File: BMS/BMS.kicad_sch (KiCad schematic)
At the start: 112 parts, among them IC1 L9963E-TR, T1 Transformer_1P_1S, T2 Transformer_1P_1S, U1 QRE1113GR

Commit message: Setting up footprint and model library
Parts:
- removed RDIS14: 39, symbol Device:R_US
- removed RLPF14, RLPF15: 100, symbol Device:R_US
- added R1, R2: 100, symbol test:RC0603FR-07100RL
- added R3: 39, symbol 39R0603:RC0603FR-0739RL
- IC1: footprint QFP50P1200X1200X120-65N -> R4_standard_footprints:QFP50P1200X1200X120-65N
- renumbered 10uf to 10uf1, 33pf to 33pf1, 4.7uf to 4.7uf1, 68nf to 68nf1, CBAT_3 to CBAT_1, CBAT_1 to CBAT_3, CBOOT to CBOOT1, CESD15 to CESD1, CESD4 to CESD10, CESD3 to CESD11, CESD5 to CESD12, CESD17 to CESD13, CESD2 to CESD14, CESD12 to CESD15, CESD7 to CESD16, CESD13 to CESD17, CESD16 to CESD2, CESD11 to CESD3, CESD10 to CESD4, CESD9 to CESD5, CESD8 to CESD6, CESD6 to CESD7, CESD18 to CESD8, CESD19 to CESD9, CFLTH to CFLTH1, CLPF13 to CLPF1, CLPF4 to CLPF10, CLPF5 to CLPF11, CLPF10 to CLPF12, CLPF6 to CLPF13, CLPF12 to CLPF2, CLPF11 to CLPF3, CLPF1 to CLPF4, CLPF2 to CLPF5, CLPF7 to CLPF6, CLPF3 to CLPF7, CNPN to CNPN1, CNTC to CNTC1, CNTC4 to CNTC3, CNTC5 to CNTC4, CNTC1 to CNTC5, CNTC3 to CNTC6, CNTC6 to CNTC7, CVANA to CVANA1, CVCOM to CVCOM1, CVTREF to CVTREF1, DOPT to DOPT1, DZBAT to DZBAT1, DZBAT to DZBAT2, FR_BAT to FR_BAT1, MREG to MREG1, RBAT_DOWN to RBAT_DOWN1, RBAT_UP to RBAT_UP1, RDIS4 to RDIS10, RDIS5 to RDIS11, RDIS3 to RDIS12, RDIS2 to RDIS13, RDIS1 to RDIS14, RDIS12 to RDIS2, RDIS13 to RDIS3, RDIS10 to RDIS4, RDIS11 to RDIS5, RDIS8 to RDIS6, RDIS9 to RDIS7, RDIS6 to RDIS8, RDIS7 to RDIS9, RFAULTL to RFAULTL1, RFAULT_DOWN to RFAULT_DOWN1, RFLT to RFLT1, RFLT_PD to RFLT_PD1, RGPIO to RGPIO1, RGPIO4 to RGPIO3, RGPIO5 to RGPIO4, RGPIO1 to RGPIO5, RGPIO3 to RGPIO6, RGPIO6 to RGPIO7, RI_Sense to RI_Sense1, RI_Sense1 to RI_Sense2, RLPF4 to RLPF10, RLPF3 to RLPF11, RLPF2 to RLPF12, RLPF1 to RLPF13, RLPF12 to RLPF14, RLPF9 to RLPF2, RLPF13 to RLPF3, RLPF8 to RLPF4, RLPF7 to RLPF5, RLPF11 to RLPF6, RLPF6 to RLPF7, RLPF10 to RLPF8, RLPF5 to RLPF9, RTERM to RTERM2, RVTREF4 to RVTREF1, RVTREF3 to RVTREF2, RVTREF2 to RVTREF3, RVTREF to RVTREF4, RVTREF6 to RVTREF5, RVTREF5 to RVTREF6, RVTREF1 to RVTREF7, T2 to T1, T1 to T2
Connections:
- net at CLPF1.2, CLPF2.1, IC1.57 (C13): now also R2.1
- net at CESD3.1, IC1.59 (B14_13): now also R2.2
- net at CESD15.1, FR_BAT1.2, RBAT_UP1.1: now also R1.2, R3.2
- net at IC1.60 (S14): now also R3.1
- net at CLPF1.1, IC1.61 (C14): now also R1.1
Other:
- moved on the sheet: CBAT_1, CBAT_2, CBAT_3, DZBAT2, FR_BAT1, RBAT_UP1

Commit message: setting up footprints and models (incomplete)
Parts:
- R1, R2: footprint (none) -> R4_standard_footprints:100R-RC0603N_YAG
- R3: footprint (none) -> R4_standard_footprints:39R-RC0603N_YAG
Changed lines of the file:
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@@
 			)
 		)
-		(property "Footprint" ""
+		(property "Footprint" "R4_standard_footprints:39R-RC0603N_YAG"
 			(at 149.86 55.88 0)
 			(effects
@@
 			)
 		)
-		(property "Footprint" ""
+		(property "Footprint" "R4_standard_footprints:100R-RC0603N_YAG"
 			(at 151.13 60.96 0)
 			(effects
@@
 			)
 		)
-		(property "Footprint" ""
+		(property "Footprint" "R4_standard_footprints:100R-RC0603N_YAG"
 			(at 149.86 50.8 0)
 			(effects

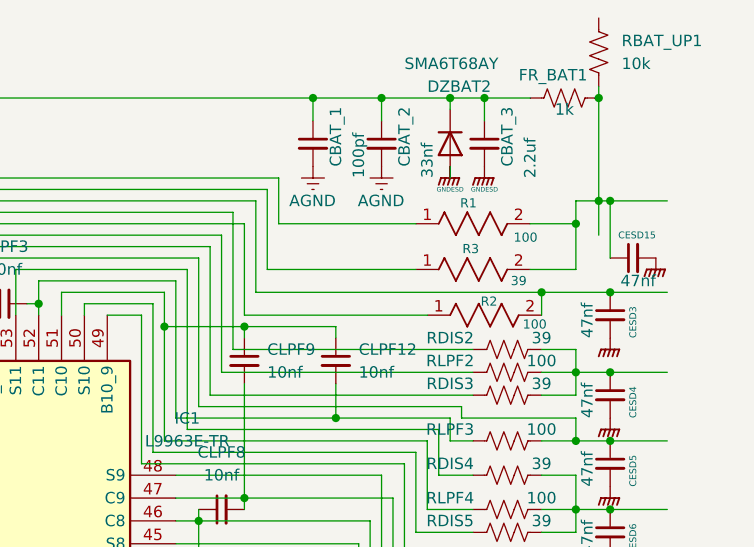
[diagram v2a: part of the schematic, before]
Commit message: Footprint set-up (mostly complete)
Finished setting up some footprints for the resistors (39 and 100)
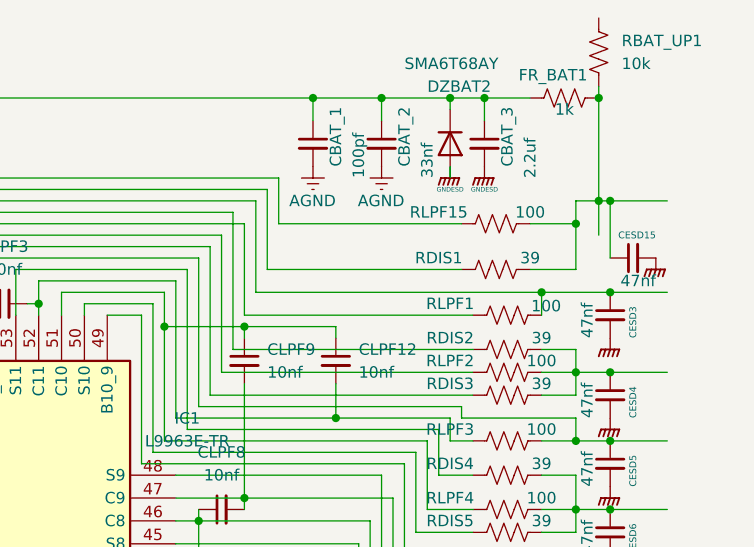
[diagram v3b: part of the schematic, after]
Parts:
- removed R1, R2: 100, R4_standard_footprints:100R-RC0603N_YAG, symbol test:RC0603FR-07100RL
- removed R3: 39, R4_standard_footprints:39R-RC0603N_YAG, symbol 39R0603:RC0603FR-0739RL
- added RDIS1: 39, R4_standard_footprints:39R-RC0603N_YAG, symbol Device:R_US
- added RLPF1, RLPF15: 100, R4_standard_footprints:100R-RC0603N_YAG, symbol Device:R_US
- RDIS10, RDIS11, RDIS12, RDIS13, RDIS14, RDIS2, RDIS3, RDIS4, RDIS5, RDIS6, RDIS7, RDIS8, RDIS9: footprint (none) -> R4_standard_footprints:39R-RC0603N_YAG
- RI_Sense1, RI_Sense2, RLPF10, RLPF11, RLPF12, RLPF13, RLPF14, RLPF2, RLPF3, RLPF4, RLPF5, RLPF6, RLPF7, RLPF8, RLPF9: footprint (none) -> R4_standard_footprints:100R-RC0603N_YAG
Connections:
- net at CESD15.1, FR_BAT1.2, RBAT_UP1.1: now also RDIS1.2, RLPF15.2
- net at IC1.60 (S14): now also RDIS1.1
- net at CLPF1.2, CLPF2.1, IC1.57 (C13): now also RLPF1.1
- net at CESD3.1, IC1.59 (B14_13): now also RLPF1.2
- net at CLPF1.1, IC1.61 (C14): now also RLPF15.1

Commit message: Fixing Schematic issues
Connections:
- net AGND: no longer CESD1.1, CESD17.1, IC1.25 (GNDREF), IC1.6 (CGND), IC1.65 (GND), IC1.9 (DGND), RDIS14.2, RI_Sense1.2, RLPF13.2, U1.2 (K)
- new net GND: CESD1.1, CESD17.1, IC1.25 (GNDREF), IC1.6 (CGND), IC1.65 (GND), IC1.9 (DGND), RDIS14.2, RI_Sense1.2, RLPF13.2, U1.2 (K)
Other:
- note added: "bruh"
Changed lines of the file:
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@@
 	)
 	(junction
-		(at 74.93 152.4)
-		(diameter 0)
-		(color 0 0 0 0)
-	)
-	(junction
 		(at 158.75 48.26)
 		(diameter 0)
@@
 	)
 	(junction
-		(at 74.93 158.75)
-		(diameter 0)
-		(color 0 0 0 0)
-	)
-	(junction
 		(at 158.75 142.24)
 		(diameter 0)
@@
 	(wire
 		(pts
-			(xy 52.07 158.75) (xy 74.93 158.75)
+			(xy 52.07 158.75) (xy 82.55 158.75)
 		)
 		(stroke
@@
 	(wire
 		(pts
-			(xy 74.93 137.16) (xy 74.93 152.4)
-		)
-		(stroke
-			(width 0)
-			(type default)
-		)
-	)
-	(wire
-		(pts
 			(xy 41.91 172.72) (xy 41.91 175.26)
 		)
@@
 	(wire
 		(pts
-			(xy 74.93 158.75) (xy 82.55 158.75)
-		)
-		(stroke
-			(width 0)
-			(type default)
-		)
-	)
-	(wire
-		(pts
 			(xy 97.79 148.59) (xy 97.79 149.86)
 		)
@@
 	(wire
 		(pts
+			(xy 46.99 88.9) (xy 49.53 88.9)
+		)
+		(stroke
+			(width 0)
+			(type default)
+		)
+	)
+	(wire
+		(pts
 			(xy 151.13 113.03) (xy 154.94 113.03)
 		)
@@
 	(wire
 		(pts
-			(xy 74.93 152.4) (xy 74.93 158.75)
-		)
-		(stroke
-			(width 0)
-			(type default)
-		)
-	)
-	(wire
-		(pts
 			(xy 85.09 59.69) (xy 86.36 59.69)
 		)
@@
 	(wire
 		(pts
+			(xy 74.93 137.16) (xy 74.93 149.86)
+		)
+		(stroke
+			(width 0)
+			(type default)
+		)
+	)
+	(wire
+		(pts
 			(xy 102.87 137.16) (xy 114.3 137.16)
 		)
@@
 	(wire
 		(pts
+			(xy 49.53 99.06) (xy 52.07 99.06)
+		)
+		(stroke
+			(width 0)
+			(type default)
+		)
+	)
+	(wire
+		(pts
 			(xy 119.38 58.42) (xy 151.13 58.42)
 		)
@@
 		)
 	)
+	(text "bruh"
+		(exclude_from_sim no)
+		(at 74.168 156.21 0)
+		(effects
+			(font
+				(size 1.27 1.27)
+			)
+		)
+	)
 	(text "Unknown GND type\n\n"
 		(exclude_from_sim no)
@@
 	)
 	(symbol
-		(lib_id "power:GNDREF")
-		(at 74.93 152.4 90)
-		(unit 1)
-		(exclude_from_sim no)
-		(in_bom yes)
-		(on_board yes)
-		(dnp no)
-		(property "Reference" "#PWR020"
-			(at 81.28 152.4 0)
-			(effects
-				(font
-					(size 1.27 1.27)
-				)
-				(hide yes)
-			)
-		)
-		(property "Value" "AGND"
-			(at 78.74 149.86 0)
-			(effects
-				(font
-					(size 1.27 1.27)
-				)
-				(justify right)
-			)
-		)
-		(property "Footprint" ""
-			(at 74.93 152.4 0)
-			(effects
-				(font
-					(size 1.27 1.27)
-				)
-				(hide yes)
-			)
-		)
-		(property "Datasheet" ""
-			(at 74.93 152.4 0)
-			(effects
-				(font
-					(size 1.27 1.27)
-				)
-				(hide yes)
-			)
-		)
-		(property "Description" "Power symbol creates a global label with name \"GNDREF\" , reference supply ground"
-			(at 74.93 152.4 0)
-			(effects
-				(font
-					(size 1.27 1.27)
-				)
-				(hide yes)
-			)
-		)
-		(pin "1"
-		)
-		(instances
-			(project ""
-				(path "/f80f938a-6d18-43c0-9c0c-cde2e6b97c6c"
-					(reference "#PWR020")
-					(unit 1)
-				)
-			)
-		)
-	)
-	(symbol
 		(lib_id "Device:C_Small")
 		(at 118.11 66.04 0)
@@
 	(symbol
 		(lib_id "power:GNDREF")
-		(at 49.53 88.9 270)
+		(at 46.99 88.9 0)
 		(unit 1)
 		(exclude_from_sim no)
@@
 		(dnp no)
 		(property "Reference" "#PWR014"
-			(at 43.18 88.9 0)
+			(at 46.99 95.25 0)
 			(effects
 				(font
@@
 		)
 		(property "Value" "AGND"
-			(at 45.72 91.44 0)
+			(at 49.53 92.71 0)
 			(effects
 				(font
@@
 		)
 		(property "Footprint" ""
-			(at 49.53 88.9 0)
+			(at 46.99 88.9 0)
 			(effects
 				(font
@@
 		)
 		(property "Datasheet" ""
-			(at 49.53 88.9 0)
+			(at 46.99 88.9 0)
 			(effects
 				(font
@@
 		)
 		(property "Description" "Power symbol creates a global label with name \"GNDREF\" , reference supply ground"
-			(at 49.53 88.9 0)
+			(at 46.99 88.9 0)
 			(effects
 				(font
@@
 		(dnp no)
 		(property "Reference" "CVCOM1"
-			(at 49.53 92.71 90)
+			(at 53.848 87.376 90)
 			(effects
 				(font
@@
 		)
 		(property "Value" "220nf"
-			(at 53.34 91.44 90)
+			(at 54.102 90.932 90)
 			(effects
 				(font
@@
 	)
 	(symbol
+		(lib_id "power:GNDREF")
+		(at 74.93 149.86 0)
+		(unit 1)
+		(exclude_from_sim no)
+		(in_bom yes)
+		(on_board yes)
+		(dnp no)
+		(property "Reference" "#PWR020"
+			(at 74.93 156.21 0)
+			(effects
+				(font
+					(size 1.27 1.27)
+				)
+				(hide yes)
+			)
+		)
+		(property "Value" "AGND"
+			(at 77.47 153.67 0)
+			(effects
+				(font
+					(size 1.27 1.27)
+				)
+				(justify right)
+			)
+		)
+		(property "Footprint" ""
+			(at 74.93 149.86 0)
+			(effects
+				(font
+					(size 1.27 1.27)
+				)
+				(hide yes)
+			)
+		)
+		(property "Datasheet" ""
+			(at 74.93 149.86 0)
+			(effects
+				(font
+					(size 1.27 1.27)
+				)
+				(hide yes)
+			)
+		)
+		(property "Description" "Power symbol creates a global label with name \"GNDREF\" , reference supply ground"
+			(at 74.93 149.86 0)
+			(effects
+				(font
+					(size 1.27 1.27)
+				)
+				(hide yes)
+			)
+		)
+		(pin "1"
+		)
+		(instances
+			(project "BMS"
+				(path "/f80f938a-6d18-43c0-9c0c-cde2e6b97c6c"
+					(reference "#PWR020")
+					(unit 1)
+				)
+			)
+		)
+	)
+	(symbol
 		(lib_id "Device:R_US")
 		(at 30.48 102.87 180)
@@
 	(symbol
 		(lib_id "power:GND")
-		(at 52.07 99.06 270)
+		(at 49.53 99.06 0)
 		(unit 1)
 		(exclude_from_sim no)
@@
 		(fields_autoplaced yes)
 		(property "Reference" "#PWR015"
-			(at 45.72 99.06 0)
+			(at 49.53 105.41 0)
 			(effects
 				(font
@@
 		)
 		(property "Value" "GND"
-			(at 48.26 99.0599 90)
+			(at 49.53 104.14 0)
 			(effects
 				(font
 					(size 1.27 1.27)
 				)
-				(justify right)
 			)
 		)
 		(property "Footprint" ""
-			(at 52.07 99.06 0)
+			(at 49.53 99.06 0)
 			(effects
 				(font
@@
 		)
 		(property "Datasheet" ""
-			(at 52.07 99.06 0)
+			(at 49.53 99.06 0)
 			(effects
 				(font
@@
 		)
 		(property "Description" "Power symbol creates a global label with name \"GND\" , ground"
-			(at 52.07 99.06 0)
+			(at 49.53 99.06 0)
 			(effects
 				(font
